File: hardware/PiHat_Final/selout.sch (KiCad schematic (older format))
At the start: 1 part, among them J2 RPi_GPIO

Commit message: Began work on RX/TX schematic.
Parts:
- removed J2: RPi_GPIO, RPi_Hat:Pin_Header_Straight_2x20, symbol RPi_GPIO
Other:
- note removed: "Thru-Hole Connector"
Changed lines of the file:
@@
 $Descr A4 11693 8268
 encoding utf-8
-Sheet 2 6
+Sheet 1 6
 Title ""
 Date ""
@@
 Comment4 ""
 $EndDescr
-$Comp
-L RPi_GPIO J2
-U 1 1 5516AE26
-P 7500 2700
-F 0 "J2" H 8250 2950 60  0000 C CNN
-F 1 "RPi_GPIO" H 8250 2850 60  0000 C CNN
-F 2 "RPi_Hat:Pin_Header_Straight_2x20" H 7500 2700 60  0001 C CNN
-F 3 "" H 7500 2700 60  0000 C CNN
-	1    7500 2700
-	1    0    0    -1
-$EndComp
-Text Notes 7800 5000 0    60   Italic 0
-Thru-Hole Connector
 $EndSCHEMATC

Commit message: Added more to the Schematic.
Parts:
- added J1: SMACONN, symbol SMACONN
- added U6: SKY13374, RFBRD:QFN_12_2mmx2mm_0.5PITCH, symbol SKY13374
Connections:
- new net: J1.1 (Rin), U6.2 (RF1)
- new net +3V3: U6.9 (VBAT)
- new net GND: J1.2 (GND), U6.10 (GND), U6.12 (GND), U6.3 (GND), U6.4 (GND), U6.6 (GND)
- new net RXI: U6.5 (RF3)
- new net SEL_1: U6.7 (V1)
- new net SEL_2: U6.8 (V2)
- new net TX_PWR: U6.11 (RF2)
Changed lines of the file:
@@
 $Descr A4 11693 8268
 encoding utf-8
-Sheet 1 6
+Sheet 6 6
 Title ""
 Date ""
@@
 Comment4 ""
 $EndDescr
+$Comp
+L SKY13374 U6
+U 1 1 58EEFD37
+P 3200 3600
+F 0 "U6" H 3200 2950 60  0000 C CNN
+F 1 "SKY13374" H 3200 4250 60  0000 C CNN
+F 2 "RFBRD:QFN_12_2mmx2mm_0.5PITCH" H 3150 3600 60  0001 C CNN
+F 3 "" H 3150 3600 60  0001 C CNN
+	1    3200 3600
+	1    0    0    -1
+$EndComp
+Wire Wire Line
+	3700 4100 3900 4100
+Wire Wire Line
+	2700 3500 2500 3500
+Wire Wire Line
+	2500 3500 2500 4200
+$Comp
+L GND #PWR46
+U 1 1 58EEFDE7
+P 2500 4200
+F 0 "#PWR46" H 2500 3950 50  0001 C CNN
+F 1 "GND" H 2500 4050 50  0000 C CNN
+F 2 "" H 2500 4200 50  0000 C CNN
+F 3 "" H 2500 4200 50  0000 C CNN
+	1    2500 4200
+	1    0    0    -1
+$EndComp
+Wire Wire Line
+	2700 4100 2500 4100
+Connection ~ 2500 4100
+Wire Wire Line
+	2700 3700 2500 3700
+Connection ~ 2500 3700
+Wire Wire Line
+	3900 3700 3900 4200
+Wire Wire Line
+	3700 3700 3900 3700
+Connection ~ 3900 4100
+$Comp
+L GND #PWR48
+U 1 1 58EEFE2B
+P 3900 4200
+F 0 "#PWR48" H 3900 3950 50  0001 C CNN
+F 1 "GND" H 3900 4050 50  0000 C CNN
+F 2 "" H 3900 4200 50  0000 C CNN
+F 3 "" H 3900 4200 50  0000 C CNN
+	1    3900 4200
+	1    0    0    -1
+$EndComp
+Wire Wire Line
+	3700 3900 4000 3900
+Wire Wire Line
+	2700 3900 2400 3900
+Text GLabel 4000 3900 2    60   Input ~ 0
+TX_PWR
+Text GLabel 2400 3900 0    60   Input ~ 0
+RXI
+Wire Wire Line
+	3700 3100 3800 3100
+Wire Wire Line
+	3700 3300 4100 3300
+Text GLabel 3800 3100 2    60   Input ~ 0
+SEL_1
+Text GLabel 4100 3300 2    60   Input ~ 0
+SEL_2
+Wire Wire Line
+	3700 3500 3800 3500
+$Comp
+L +3V3 #PWR47
+U 1 1 58EEFEEA
+P 3800 3500
+F 0 "#PWR47" H 3800 3350 50  0001 C CNN
+F 1 "+3V3" H 3800 3640 50  0000 C CNN
+F 2 "" H 3800 3500 50  0000 C CNN
+F 3 "" H 3800 3500 50  0000 C CNN
+	1    3800 3500
+	1    0    0    -1
+$EndComp
+Wire Wire Line
+	2700 3300 2000 3300
+$Comp
+L SMACONN J1
+U 1 1 58EEFF3A
+P 1600 3400
+F 0 "J1" H 1600 3200 60  0000 C CNN
+F 1 "SMACONN" H 1600 3600 60  0000 C CNN
+F 2 "" H 1600 3400 60  0001 C CNN
+F 3 "" H 1600 3400 60  0001 C CNN
+	1    1600 3400
+	1    0    0    -1
+$EndComp
+Wire Wire Line
+	2000 3500 2100 3500
+Wire Wire Line
+	2100 3500 2100 3600
+$Comp
+L GND #PWR45
+U 1 1 58EF0036
+P 2100 3600
+F 0 "#PWR45" H 2100 3350 50  0001 C CNN
+F 1 "GND" H 2100 3450 50  0000 C CNN
+F 2 "" H 2100 3600 50  0000 C CNN
+F 3 "" H 2100 3600 50  0000 C CNN
+	1    2100 3600
+	1    0    0    -1
+$EndComp
 $EndSCHEMATC

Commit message: Began Layout, Pihat final.
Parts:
- J1: footprint (none) -> RF BW Filter:SMA_Edge_Mount
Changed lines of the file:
@@
 LIBS:contrib
 LIBS:valves
-LIBS:RFT
 LIBS:RPi_Hat-cache
 EELAYER 25 0
@@
 	2500 3500 2500 4200
 $Comp
-L GND #PWR46
+L GND #PWR045
 U 1 1 58EEFDE7
 P 2500 4200
-F 0 "#PWR46" H 2500 3950 50  0001 C CNN
+F 0 "#PWR045" H 2500 3950 50  0001 C CNN
 F 1 "GND" H 2500 4050 50  0000 C CNN
 F 2 "" H 2500 4200 50  0000 C CNN
@@
 Connection ~ 3900 4100
 $Comp
-L GND #PWR48
+L GND #PWR046
 U 1 1 58EEFE2B
 P 3900 4200
-F 0 "#PWR48" H 3900 3950 50  0001 C CNN
+F 0 "#PWR046" H 3900 3950 50  0001 C CNN
 F 1 "GND" H 3900 4050 50  0000 C CNN
 F 2 "" H 3900 4200 50  0000 C CNN
@@
 	3700 3500 3800 3500
 $Comp
-L +3V3 #PWR47
+L +3V3 #PWR047
 U 1 1 58EEFEEA
 P 3800 3500
-F 0 "#PWR47" H 3800 3350 50  0001 C CNN
+F 0 "#PWR047" H 3800 3350 50  0001 C CNN
 F 1 "+3V3" H 3800 3640 50  0000 C CNN
 F 2 "" H 3800 3500 50  0000 C CNN
@@
 F 0 "J1" H 1600 3200 60  0000 C CNN
 F 1 "SMACONN" H 1600 3600 60  0000 C CNN
-F 2 "" H 1600 3400 60  0001 C CNN
+F 2 "RF BW Filter:SMA_Edge_Mount" H 1600 3400 60  0001 C CNN
 F 3 "" H 1600 3400 60  0001 C CNN
 	1    1600 3400
@@
 	2100 3500 2100 3600
 $Comp
-L GND #PWR45
+L GND #PWR048
 U 1 1 58EF0036
 P 2100 3600
-F 0 "#PWR45" H 2100 3350 50  0001 C CNN
+F 0 "#PWR048" H 2100 3350 50  0001 C CNN
 F 1 "GND" H 2100 3450 50  0000 C CNN
 F 2 "" H 2100 3600 50  0000 C CNN

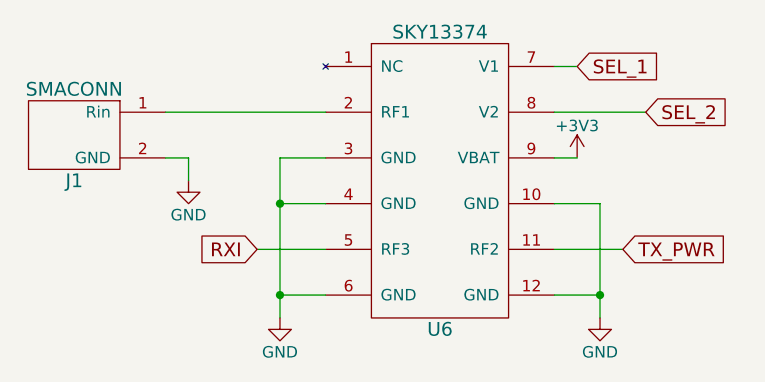
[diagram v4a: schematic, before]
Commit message: Transciever wiring & Power Distribution Changes, modified footprint for Edge SMA, swapped TX/RX on ANTSEL
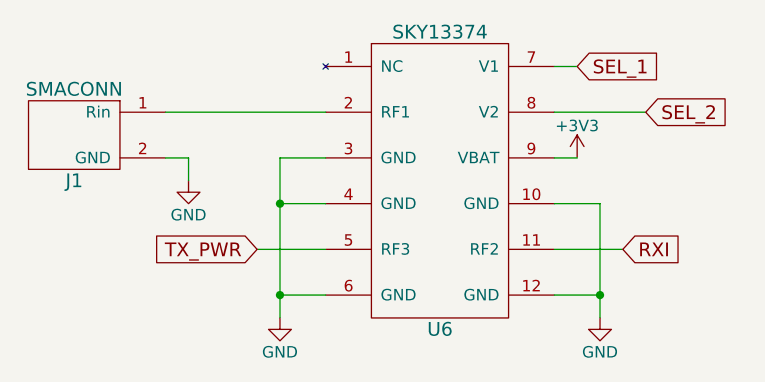
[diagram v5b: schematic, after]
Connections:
- net RXI: now also U6.11 (RF2); no longer U6.5 (RF3)
- net TX_PWR: now also U6.5 (RF3); no longer U6.11 (RF2)
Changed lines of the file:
@@
 	2500 3500 2500 4200
 $Comp
-L GND #PWR045
+L GND #PWR049
 U 1 1 58EEFDE7
 P 2500 4200
-F 0 "#PWR045" H 2500 3950 50  0001 C CNN
+F 0 "#PWR049" H 2500 3950 50  0001 C CNN
 F 1 "GND" H 2500 4050 50  0000 C CNN
 F 2 "" H 2500 4200 50  0000 C CNN
@@
 Connection ~ 3900 4100
 $Comp
-L GND #PWR046
+L GND #PWR050
 U 1 1 58EEFE2B
 P 3900 4200
-F 0 "#PWR046" H 3900 3950 50  0001 C CNN
+F 0 "#PWR050" H 3900 3950 50  0001 C CNN
 F 1 "GND" H 3900 4050 50  0000 C CNN
 F 2 "" H 3900 4200 50  0000 C CNN
@@
 	2700 3900 2400 3900
 Text GLabel 4000 3900 2    60   Input ~ 0
+RXI
+Text GLabel 2400 3900 0    60   Input ~ 0
 TX_PWR
-Text GLabel 2400 3900 0    60   Input ~ 0
-RXI
 Wire Wire Line
 	3700 3100 3800 3100
@@
 	3700 3500 3800 3500
 $Comp
-L +3V3 #PWR047
+L +3V3 #PWR051
 U 1 1 58EEFEEA
 P 3800 3500
-F 0 "#PWR047" H 3800 3350 50  0001 C CNN
+F 0 "#PWR051" H 3800 3350 50  0001 C CNN
 F 1 "+3V3" H 3800 3640 50  0000 C CNN
 F 2 "" H 3800 3500 50  0000 C CNN
@@
 	2100 3500 2100 3600
 $Comp
-L GND #PWR048
+L GND #PWR052
 U 1 1 58EF0036
 P 2100 3600
-F 0 "#PWR048" H 2100 3350 50  0001 C CNN
+F 0 "#PWR052" H 2100 3350 50  0001 C CNN
 F 1 "GND" H 2100 3450 50  0000 C CNN
 F 2 "" H 2100 3600 50  0000 C CNN
